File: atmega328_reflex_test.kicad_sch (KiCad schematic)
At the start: 6 parts, among them J1 Conn_01x04_Socket, U1 ATmega328-P, Y1 Crystal

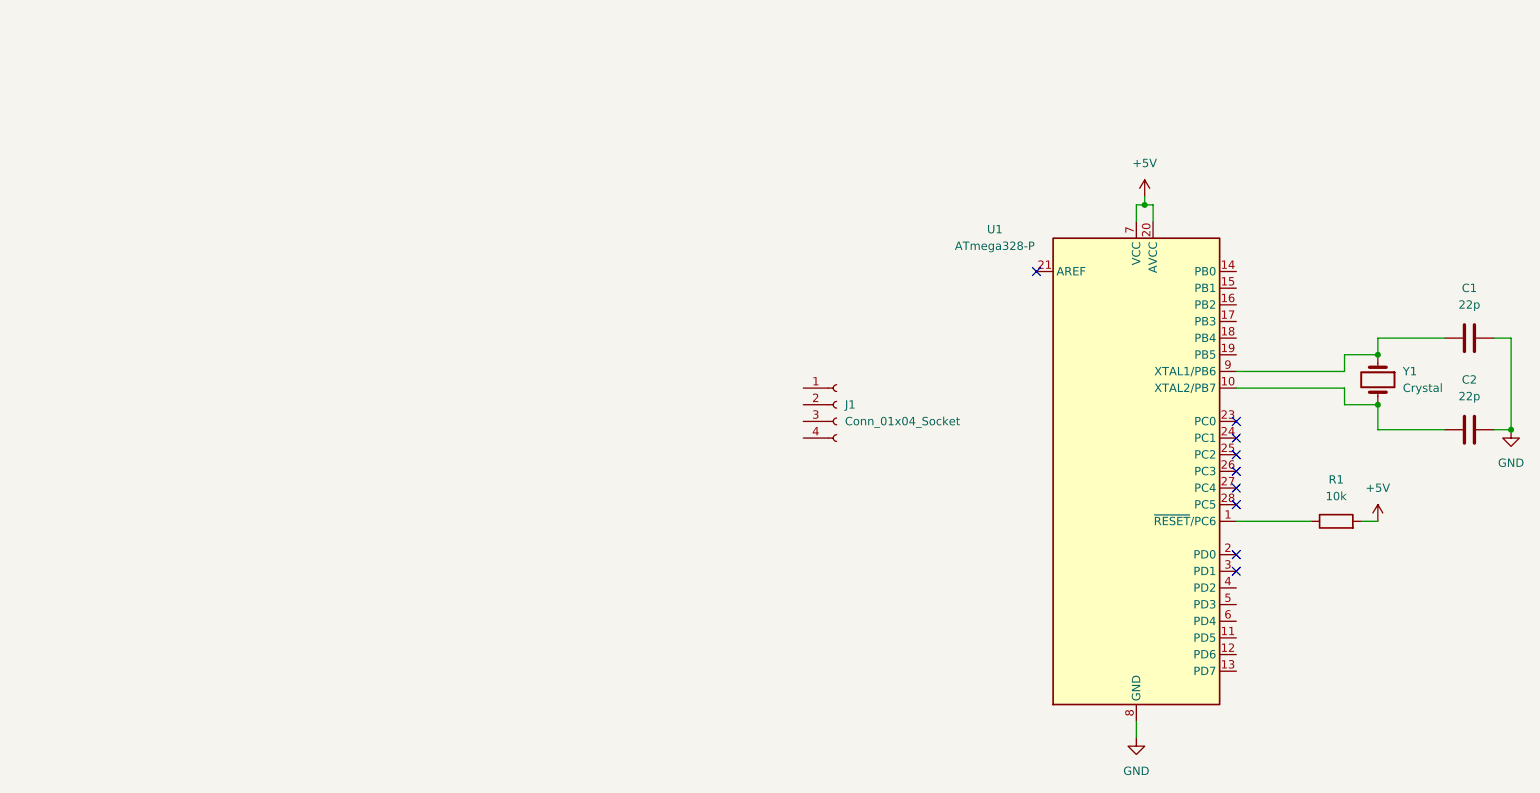
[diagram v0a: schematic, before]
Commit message: shematic without power supply
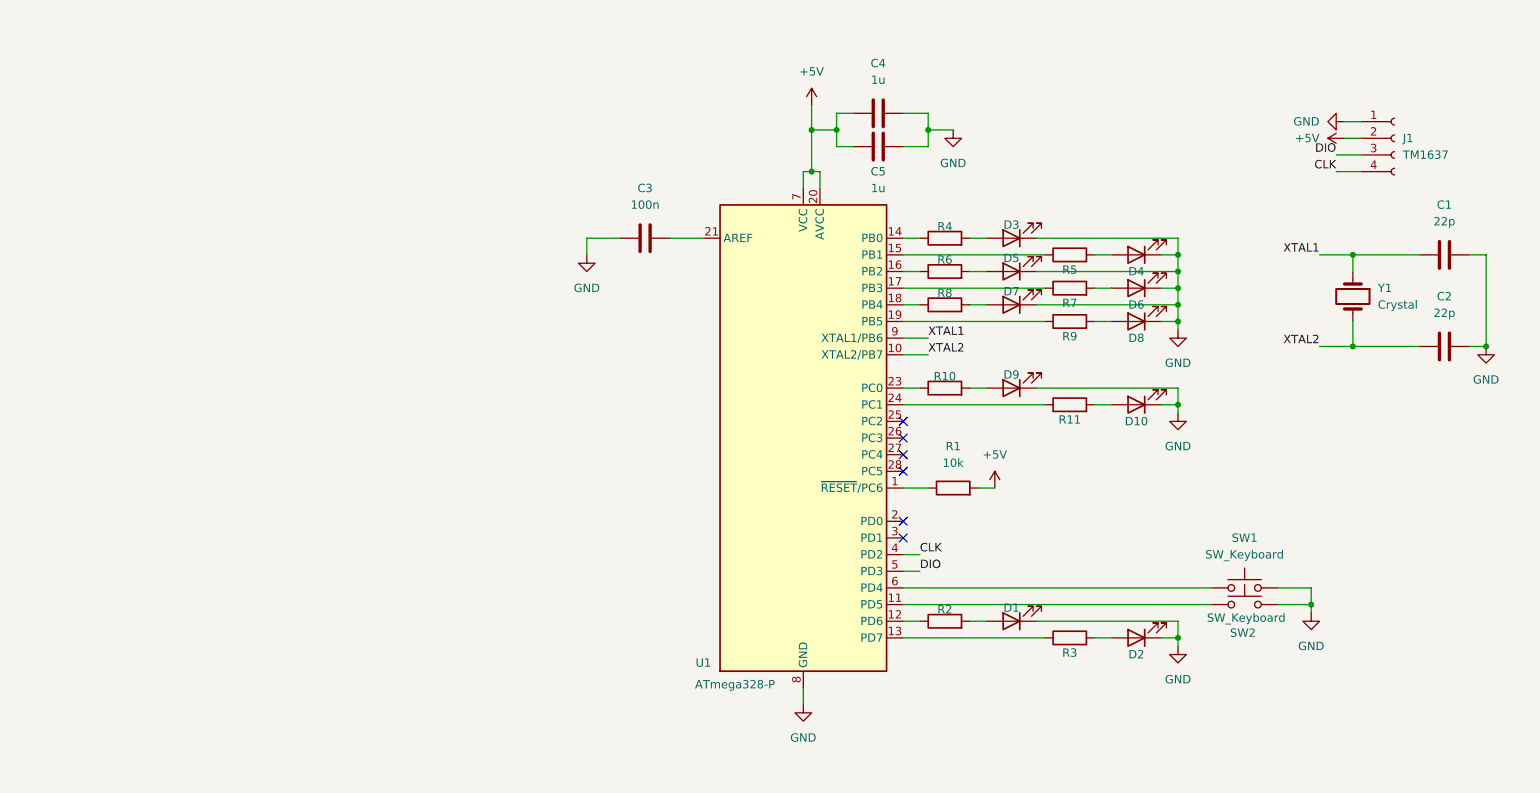
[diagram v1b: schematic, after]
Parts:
- added C3: 100n, Capacitor_THT:C_Disc_D4.3mm_W1.9mm_P5.00mm, symbol Device:C
- added C4, C5: 1u, Capacitor_THT:C_Disc_D4.3mm_W1.9mm_P5.00mm, symbol Device:C
- added D1, D2: LED, LED_THT:LED_D5.0mm, symbol Device:LED
- added D10, D3, D4, D5, D6, D7, D8, D9: LED, LED_THT:LED_D3.0mm, symbol Device:LED
- added R10, R11, R4, R5, R6, R7, R8, R9: 6k8, Resistor_THT:R_Axial_DIN0207_L6.3mm_D2.5mm_P7.62mm_Horizontal, symbol Device:R
- added R2, R3: 4k7, Resistor_THT:R_Axial_DIN0207_L6.3mm_D2.5mm_P7.62mm_Horizontal, symbol Device:R
- added SW1, SW2: SW_Keyboard, Button_Switch_Keyboard:SW_Cherry_MX_1.00u_PCB, symbol Switch:SW_Push
- C1, C2: footprint (none) -> Capacitor_THT:C_Disc_D3.0mm_W1.6mm_P2.50mm
- J1: value Conn_01x04_Socket -> TM1637
- R1: footprint (none) -> Resistor_THT:R_Axial_DIN0207_L6.3mm_D2.5mm_P7.62mm_Horizontal
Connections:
- net +5V: now also J1.2 (Pin_2), C4.1, C5.2
- net GND: now also J1.1 (Pin_1), C3.1, C4.2, C5.1, D1.1 (K), D10.1 (K), D2.1 (K), D3.1 (K), D4.1 (K), D5.1 (K), D6.1 (K), D7.1 (K), D8.1 (K), D9.1 (K), SW1.2, SW2.2
- net XTAL2: now reaches C2.1, U1.10 (XTAL2/PB7), Y1.2
- net at U1.11 (PD5): now also SW2.1
- net at U1.12 (PD6): now also R2.1
- net at U1.13 (PD7): now also R3.1
- net at U1.14 (PB0): now also R4.1
- net at U1.15 (PB1): now also R5.1
- net at U1.16 (PB2): now also R6.1
- net at U1.17 (PB3): now also R7.1
- net at U1.18 (PB4): now also R8.1
- net at U1.19 (PB5): now also R9.1
- net at U1.21 (AREF): now also C3.2
- net at U1.23 (PC0): now also R10.1
- net at U1.24 (PC1): now also R11.1
- net CLK: now reaches U1.4 (PD2)
- net CLK: now also J1.4 (Pin_4)
- net DIO: now reaches U1.5 (PD3)
- net DIO: now also J1.3 (Pin_3)
- net at U1.6 (PD4): now also SW1.1
- net XTAL1: now reaches C1.1, U1.9 (XTAL1/PB6), Y1.1
- new net: D10.2 (A), R11.2
- new net: D5.2 (A), R6.2
- new net: D2.2 (A), R3.2
- new net: D1.2 (A), R2.2
- new net: D6.2 (A), R7.2
- new net: D4.2 (A), R5.2
- new net: D8.2 (A), R9.2
- new net: D3.2 (A), R4.2
- new net: D7.2 (A), R8.2
- new net: D9.2 (A), R10.2
- no-connect marks 9 -> 6
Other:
- moved on the sheet: C1, C2, J1, R1, U1, Y1

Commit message: added power supply
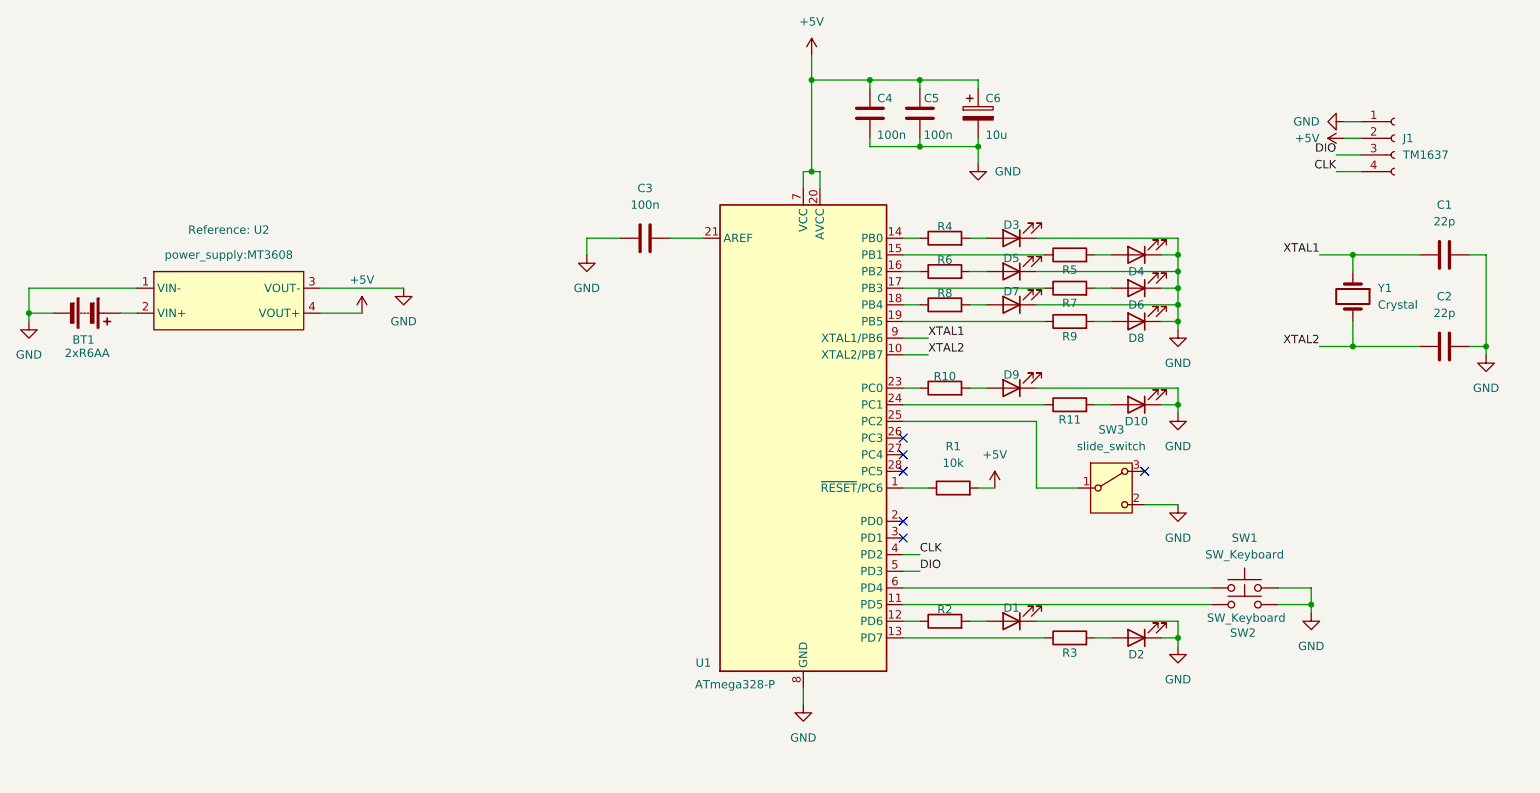
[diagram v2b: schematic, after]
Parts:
- added BT1: 2xR6AA, power_supply:2xAA_holder, symbol Device:Battery
- added C6: 10u, Capacitor_THT:CP_Radial_D8.0mm_P3.80mm, symbol Device:C_Polarized
- added SW3: slide_switch, power_supply:SW_Slide_8.6x3.8x7.0_P2.54mm, symbol Switch:SW_Wuerth_450301014042
- added U2: ~, power_supply:MT3608, symbol power_supply_sym:MT3608_module
- C4, C5: value 1u -> 100n
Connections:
- net +5V: now also C6.1, U2.4 (VOUT+)
- net GND: now also BT1.2 (-), C6.2, SW3.2 (C), U2.1 (VIN-), U2.3 (VOUT-)
- net at U1.25 (PC2): now also SW3.1 (B)
- new net: BT1.1 (+), U2.2 (VIN+)
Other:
- moved on the sheet: C4, C5

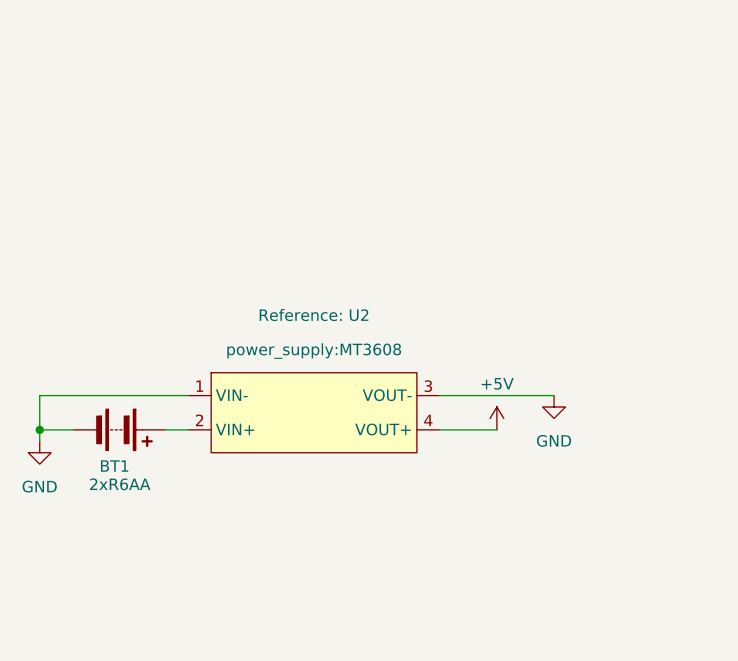
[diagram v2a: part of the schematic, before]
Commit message: finish schematic and general layout
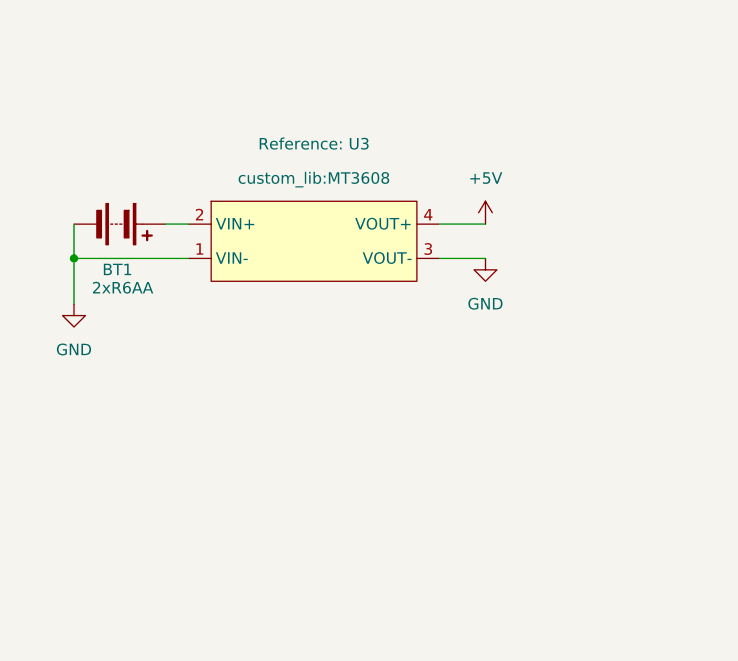
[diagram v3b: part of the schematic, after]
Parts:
- removed U2: ~, power_supply:MT3608, symbol power_supply_sym:MT3608_module
- added U3: ~, custom_lib:MT3608, symbol power_supply_sym:MT3608_module
- BT1: footprint power_supply:2xAA_holder -> custom_lib:2xAA_holder
- J1: footprint (none) -> custom_lib:HW069
- SW3: footprint power_supply:SW_Slide_8.6x3.8x7.0_P2.54mm -> custom_lib:SW_Slide_8.6x3.8x7.0_P2.54mm
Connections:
- net +5V: now also U3.4 (VOUT+)
- net GND: now also U3.1 (VIN-), U3.3 (VOUT-)
- net at BT1.1 (+): now also U3.2 (VIN+)
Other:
- moved on the sheet: BT1

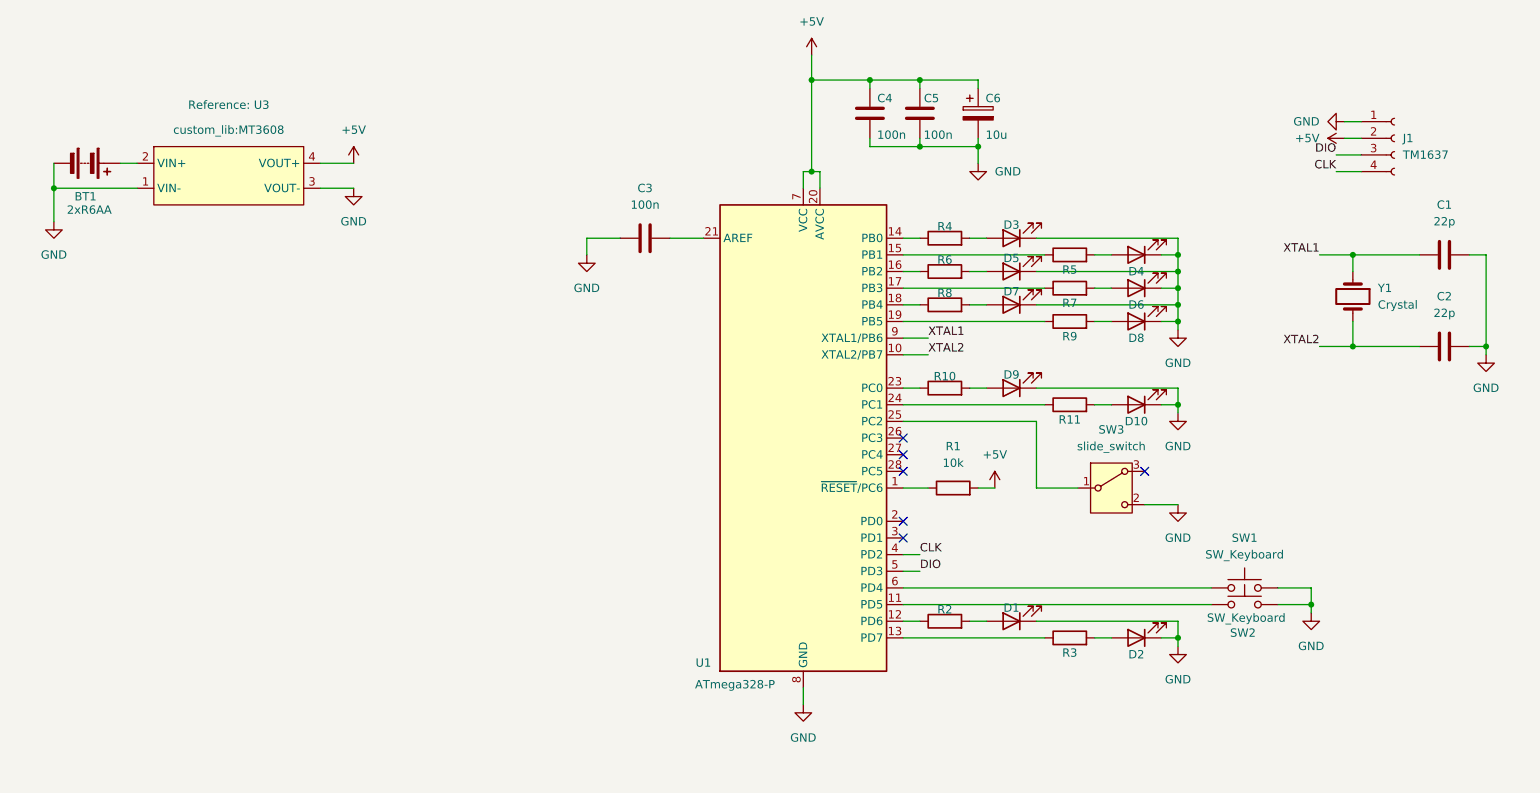
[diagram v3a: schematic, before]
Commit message: initial wiring
changed pin 4 with pin 7
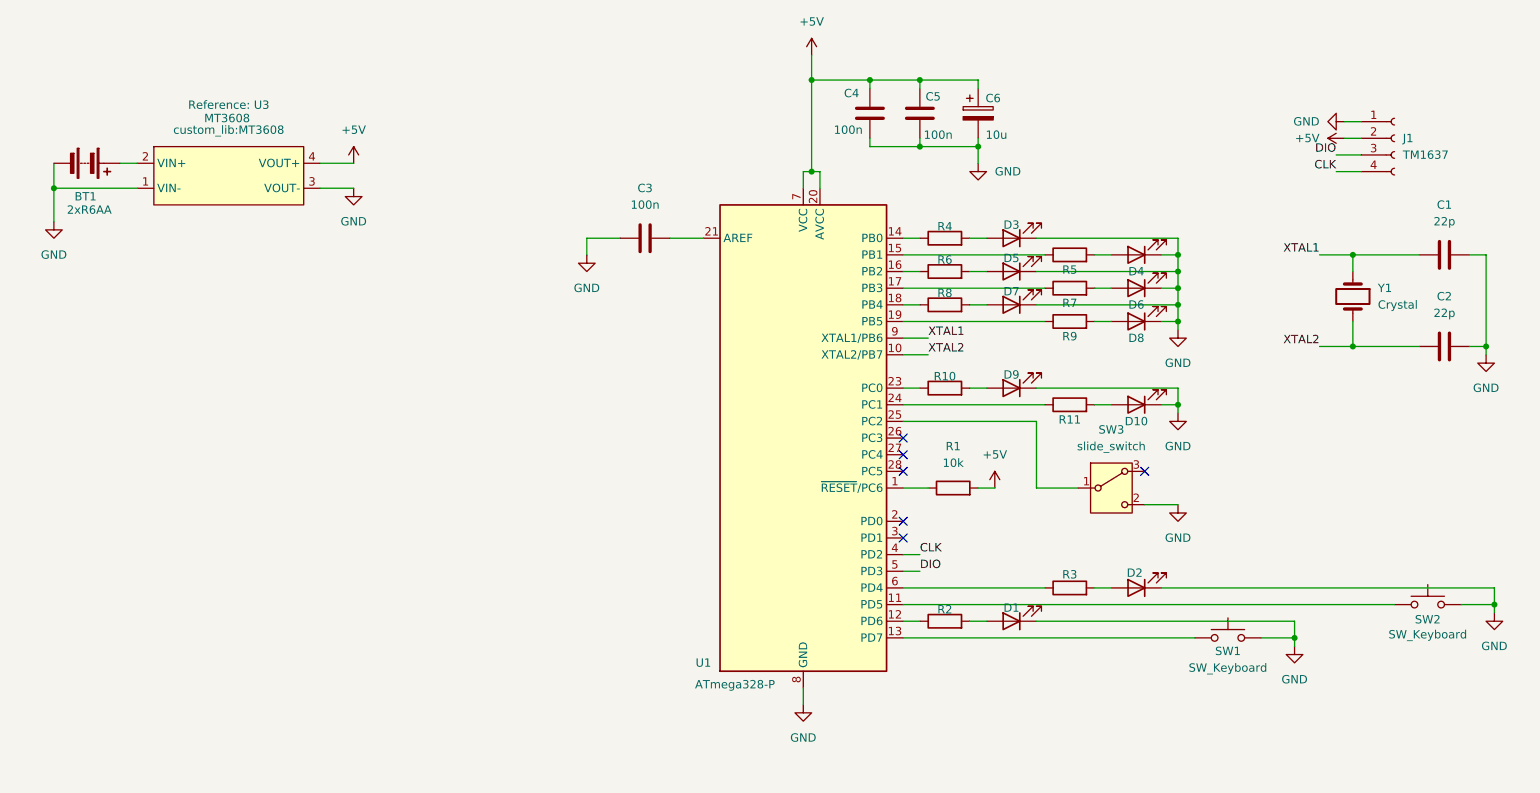
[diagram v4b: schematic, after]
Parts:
- U3: value ~ -> MT3608
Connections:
- net +5V: now also C4.2; no longer C4.1
- net GND: now also C4.1; no longer C4.2
- net at R3.1: now also U1.6 (PD4); no longer U1.13 (PD7)
- net at SW1.1: now also U1.13 (PD7); no longer U1.6 (PD4)
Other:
- moved on the sheet: C4, D2, R3, SW1, SW2

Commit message: version 1 finished
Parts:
- SW3: value slide_switch -> MULTIPLAYER
- renumbered U3 to U2
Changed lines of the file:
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@@
 		(on_board yes)
 		(dnp no)
-		(property "Reference" "U3"
+		(property "Reference" "U2"
 			(at 73.66 52.07 0)
 			(show_name yes)
@@
 			(project ""
 				(path "/91926390-6ee2-4f94-b466-10e7c61b1308"
-					(reference "U3")
+					(reference "U2")
 					(unit 1)
 				)
@@
 			)
 		)
-		(property "Value" "slide_switch"
+		(property "Value" "MULTIPLAYER"
 			(at 208.28 104.14 0)
 			(effects

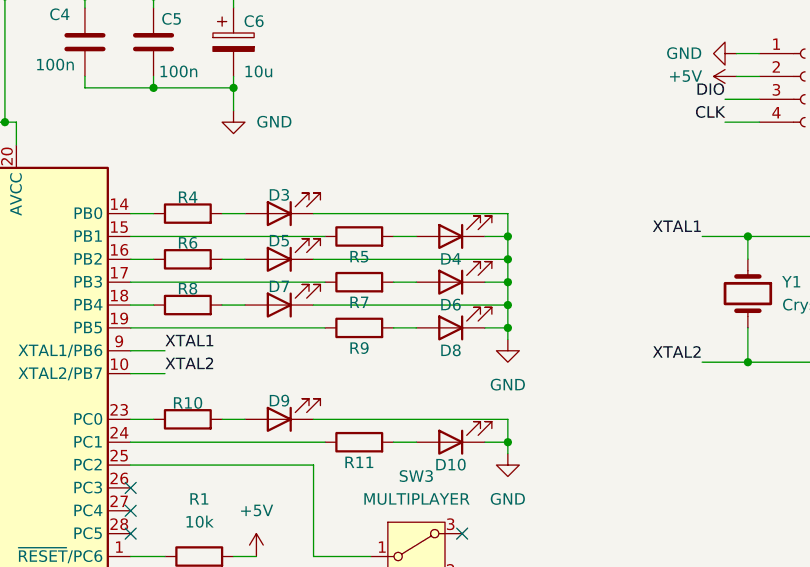
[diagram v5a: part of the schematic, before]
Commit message: update resistor values
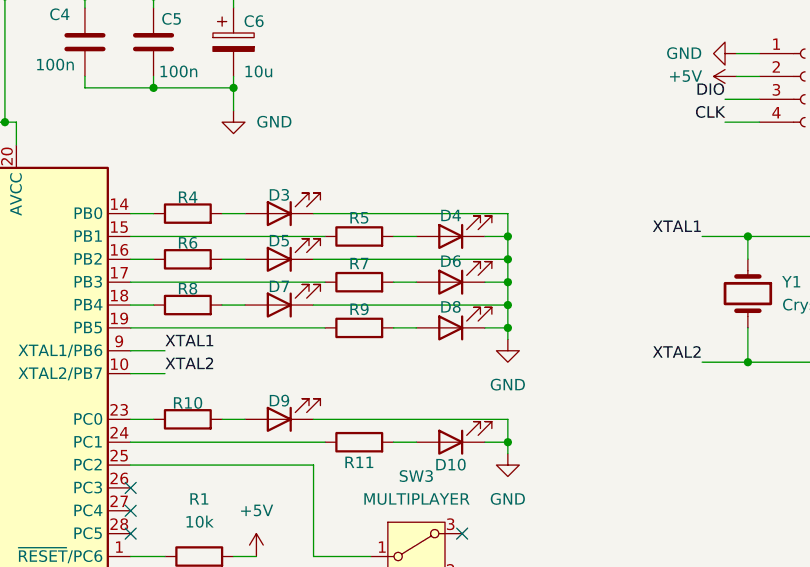
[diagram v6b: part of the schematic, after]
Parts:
- R10, R11, R4, R5, R6, R7, R8, R9: value 6k8 -> 5k1
- R2, R3: value 4k7 -> 3k3
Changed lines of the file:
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@@
 			)
 		)
-		(property "Value" "6k8"
+		(property "Value" "5k1"
 			(at 182.88 73.66 90)
 			(effects
@@
 			)
 		)
-		(property "Value" "4k7"
+		(property "Value" "3k3"
 			(at 201.93 121.92 90)
 			(effects
@@
 		(dnp no)
 		(property "Reference" "R7"
-			(at 201.93 82.296 90)
+			(at 201.93 77.978 90)
 			(effects
 				(font
@@
 			)
 		)
-		(property "Value" "6k8"
+		(property "Value" "5k1"
 			(at 201.93 76.2 90)
 			(effects
@@
 		(dnp no)
 		(property "Reference" "R5"
-			(at 201.93 77.216 90)
+			(at 201.93 72.898 90)
 			(effects
 				(font
@@
 			)
 		)
-		(property "Value" "6k8"
+		(property "Value" "5k1"
 			(at 201.93 71.12 90)
 			(effects
@@
 		(dnp no)
 		(property "Reference" "D8"
-			(at 212.09 87.63 0)
+			(at 212.09 82.804 0)
 			(effects
 				(font
@@
 			)
 		)
-		(property "Value" "6k8"
+		(property "Value" "5k1"
 			(at 182.88 91.44 90)
 			(effects
@@
 			)
 		)
-		(property "Value" "6k8"
+		(property "Value" "5k1"
 			(at 201.93 93.98 90)
 			(effects
@@
 			)
 		)
-		(property "Value" "4k7"
+		(property "Value" "3k3"
 			(at 182.88 127 90)
 			(effects
@@
 			)
 		)
-		(property "Value" "6k8"
+		(property "Value" "5k1"
 			(at 182.88 68.58 90)
 			(effects
@@
 		(dnp no)
 		(property "Reference" "D4"
-			(at 212.09 77.47 0)
+			(at 212.09 72.644 0)
 			(effects
 				(font
@@
 		(dnp no)
 		(property "Reference" "D6"
-			(at 212.09 82.55 0)
+			(at 212.09 77.724 0)
 			(effects
 				(font
@@
 		(dnp no)
 		(property "Reference" "R9"
-			(at 201.93 87.376 90)
+			(at 201.93 83.058 90)
 			(effects
 				(font
@@
 			)
 		)
-		(property "Value" "6k8"
+		(property "Value" "5k1"
 			(at 201.93 81.28 90)
 			(effects
@@
 			)
 		)
-		(property "Value" "6k8"
+		(property "Value" "5k1"
 			(at 182.88 78.74 90)
 			(effects
